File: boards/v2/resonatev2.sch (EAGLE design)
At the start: 37 parts, among them U1 CC1101RTK, Y1 26 mHz

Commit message: making a new board
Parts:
- removed C1: 10uf, adafruit:C-USC0603
- removed U$1: RFD22301, RFD22301-11.25.13:RFD22301
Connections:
- removed net N$4: U$1.GND@7, U$1.GND@8
- removed net N$5: U$1.GND@1, U$1.GND@2
- removed net N$6: C1.1, U$1.RESET
- removed net N$7: C1.2, JP2.1
- removed net N$8: JP2.2, U$1.P0.01/AIN2
- removed net N$9: JP2.3, U$1.P0.00/AREF0
- removed net P5: JP1.3, U$1.P0.05/AIN6
- new net N$2: JP1.3, U1.SO(GDO1)
- net GND: no longer JP2.6, U$1.GND@4, U$1.GND@5, U$1.GND@6
- net N$32: now also JP1.4
- net P2: no longer JP1.6, U$1.P0.02/AIN3
- net P3: no longer JP1.5, U$1.P0.03/AIN4, U1.SO(GDO1)
- net P4: now also JP1.2; no longer JP1.4, U$1.P0.04/AIN5
- net P6: now also JP1.5; no longer JP1.2, U$1.P0.06/AIN7
- net VCC: now also JP1.6; no longer JP2.4, U$1.+3.3V
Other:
- moved on the sheet: JP2

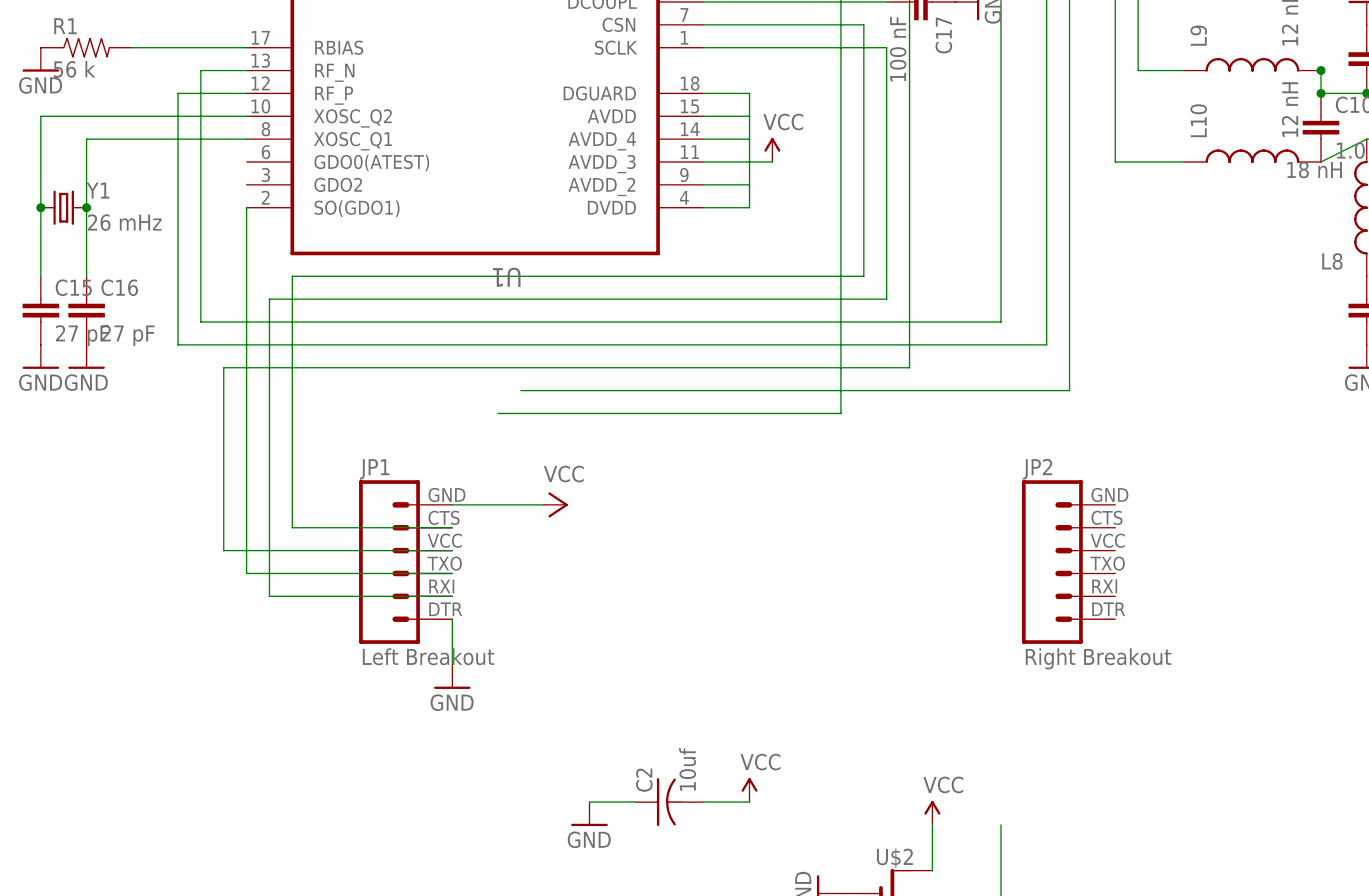
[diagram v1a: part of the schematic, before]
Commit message: adding new boards for nrf905
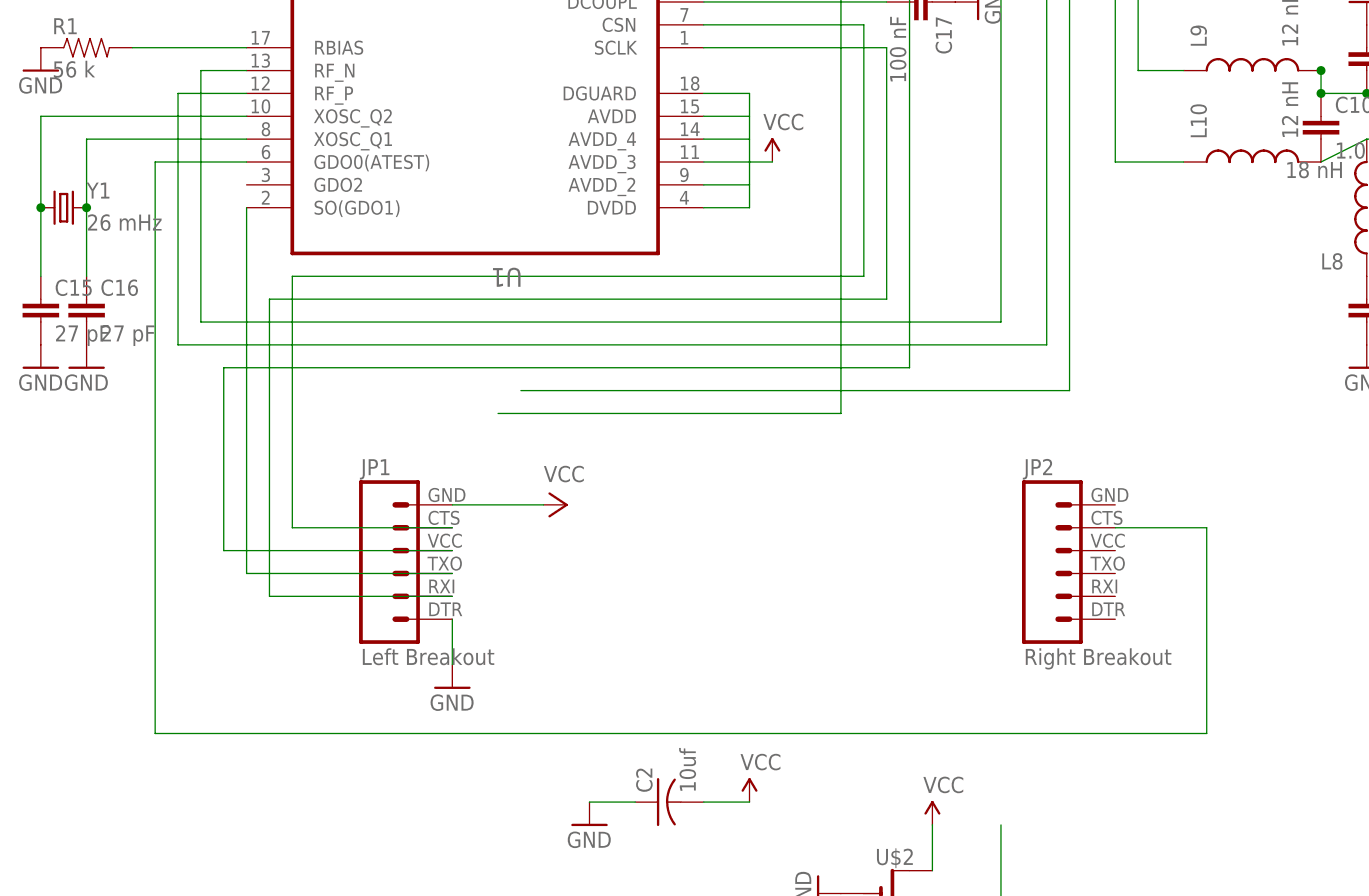
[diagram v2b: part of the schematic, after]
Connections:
- new net N$3: JP2.5, U1.GDO0(ATEST)
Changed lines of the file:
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@@
+</segment>
+</net>
+<net name="N$3" class="0">
+<segment>
+<pinref part="U1" gate="A" pin="GDO0(ATEST)"/>
+<wire x1="-27.94" y1="109.22" x2="-38.1" y2="109.22" width="0.1524" layer="91"/>
+<wire x1="-38.1" y1="109.22" x2="-38.1" y2="45.72" width="0.1524" layer="91"/>
+<wire x1="-38.1" y1="45.72" x2="78.74" y2="45.72" width="0.1524" layer="91"/>
+<wire x1="78.74" y1="45.72" x2="78.74" y2="68.58" width="0.1524" layer="91"/>
+<pinref part="JP2" gate="G$1" pin="5"/>
+<wire x1="78.74" y1="68.58" x2="68.58" y2="68.58" width="0.1524" layer="91"/>
 </segment>
 </net>
